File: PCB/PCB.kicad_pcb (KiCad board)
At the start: 2 copper layers, 97.1 x 48.7 mm, 11 parts, among them J1 Conn_01x08_Pin, SW1 SW_Push, SW2 SW_Push, SW3 SW_Push, SW4 SW_Push, U1 XIAO-ESP32-C3-SMD

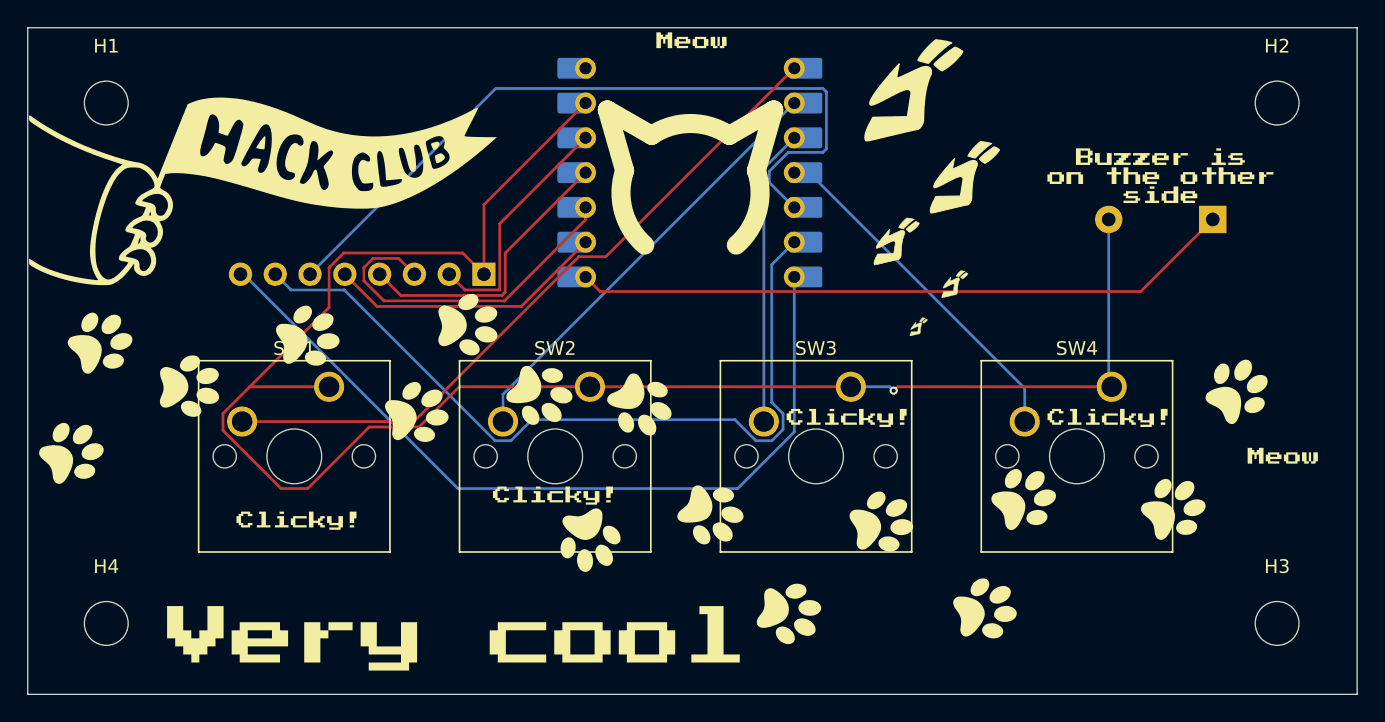
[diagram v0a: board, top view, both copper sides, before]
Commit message: Made some traces round, also firmware update a bit
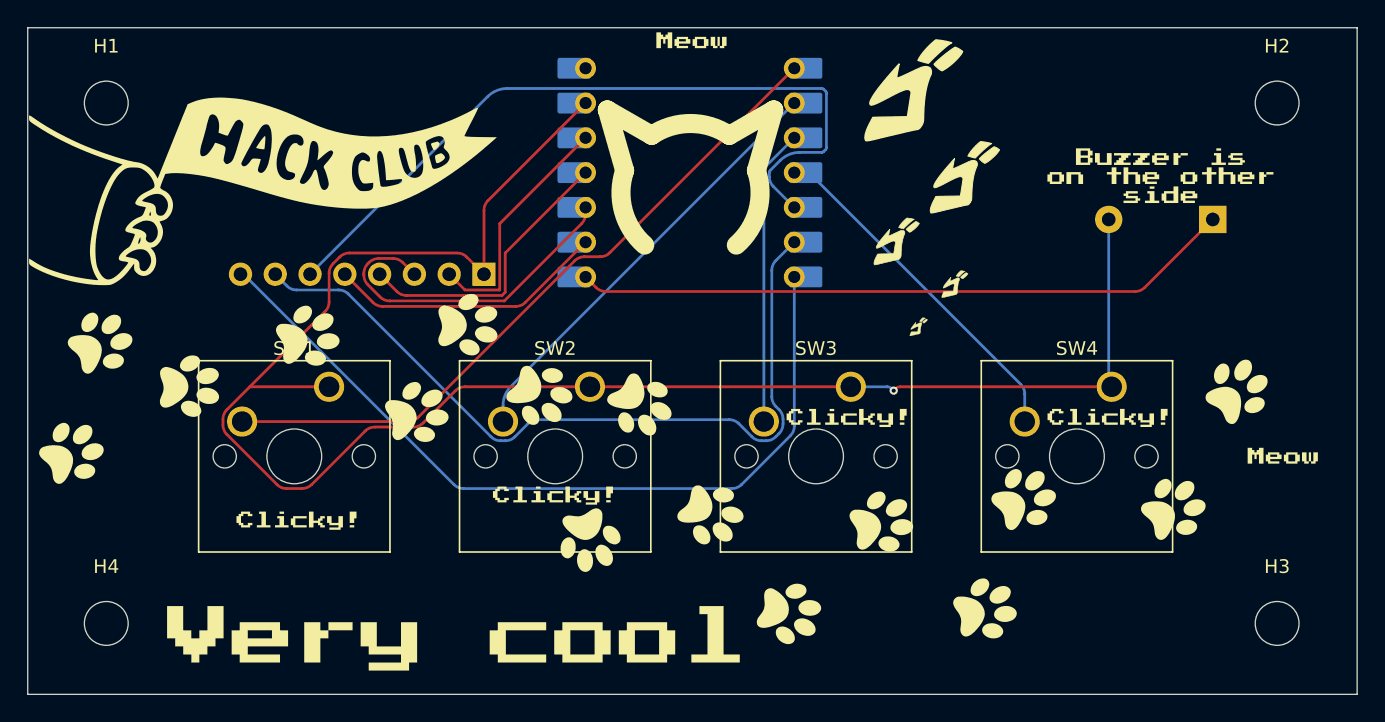
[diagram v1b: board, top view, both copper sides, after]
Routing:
- net /GND: track 131.1 -> 130.5 mm
- net /CS: track 58.4 -> 57.9 mm
